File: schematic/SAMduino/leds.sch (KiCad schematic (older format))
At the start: 22 parts, among them SW1 SW_SPST, SW2 MCLR, SW3 SW_SPST, SW4 ERASE

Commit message: Specialty pins wired
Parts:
- removed J?: Conn_02x03_Odd_Even, symbol Connector_Generic:Conn_02x03_Odd_Even
- removed J?: Conn_02x02_Odd_Even, symbol Connector_Generic:Conn_02x02_Odd_Even
- removed J?: Conn_01x03, symbol Connector_Generic:Conn_01x03
- removed J?: Conn_02x04_Odd_Even, symbol Connector_Generic:Conn_02x04_Odd_Even
- removed J?: Conn_01x04, symbol Connector_Generic:Conn_01x04
- removed J?: Conn_02x10_Top_Bottom, symbol Connector_Generic:Conn_02x10_Top_Bottom
- added J? (x3): Conn_02x03_Odd_Even, symbol Connector_Generic:Conn_02x03_Odd_Even
- added J?: Conn_01x02, symbol Connector_Generic:Conn_01x02
- added J? (x2): Conn_02x02_Odd_Even, symbol Connector_Generic:Conn_02x02_Odd_Even
- added R? (x2): 100k, symbol Device:R
- added R? (x2): 4k7, symbol Device:R
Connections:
- net labels added: AN0, AN1, AN2, DAC0, NRST, PB5, RXD0, SPI0_MISO, SPI0_MOSI, SPI0_NPCS0, SPI0_SPCK, SWCLK, SWDIO, TWCK0, TWD0, TXD0, VDD5V, VIN
- net labels removed: MCLR
- wire segments 34 -> 89
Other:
- note added: "ADC and DAC"
- note added: "Power"
- note added: "Pullup Enable"
- note added: "TWI0"
- note added: "USART0"
- note removed: "ADC, DAC, Comparator?"
- note removed: "GPIO"
- note removed: "PWM"
- note removed: "TWI0 and TWI1\n(need pullups)"
- note removed: "USART0 and UART?"
- moved on the sheet: J?, R12, SW4

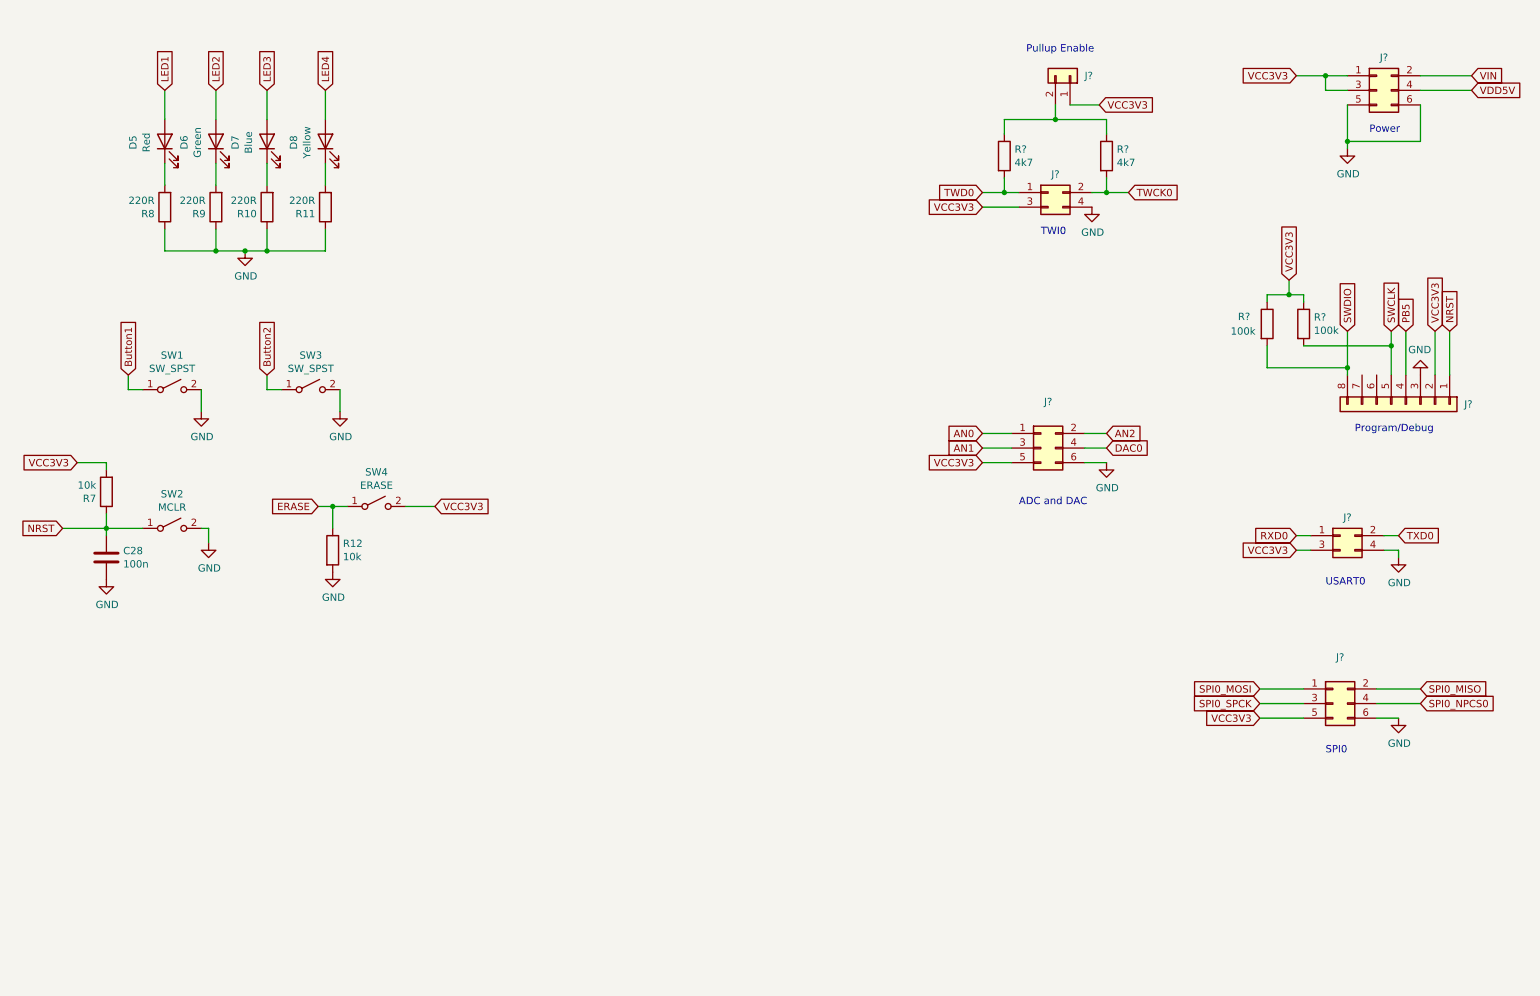
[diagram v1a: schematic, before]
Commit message: All pins connected
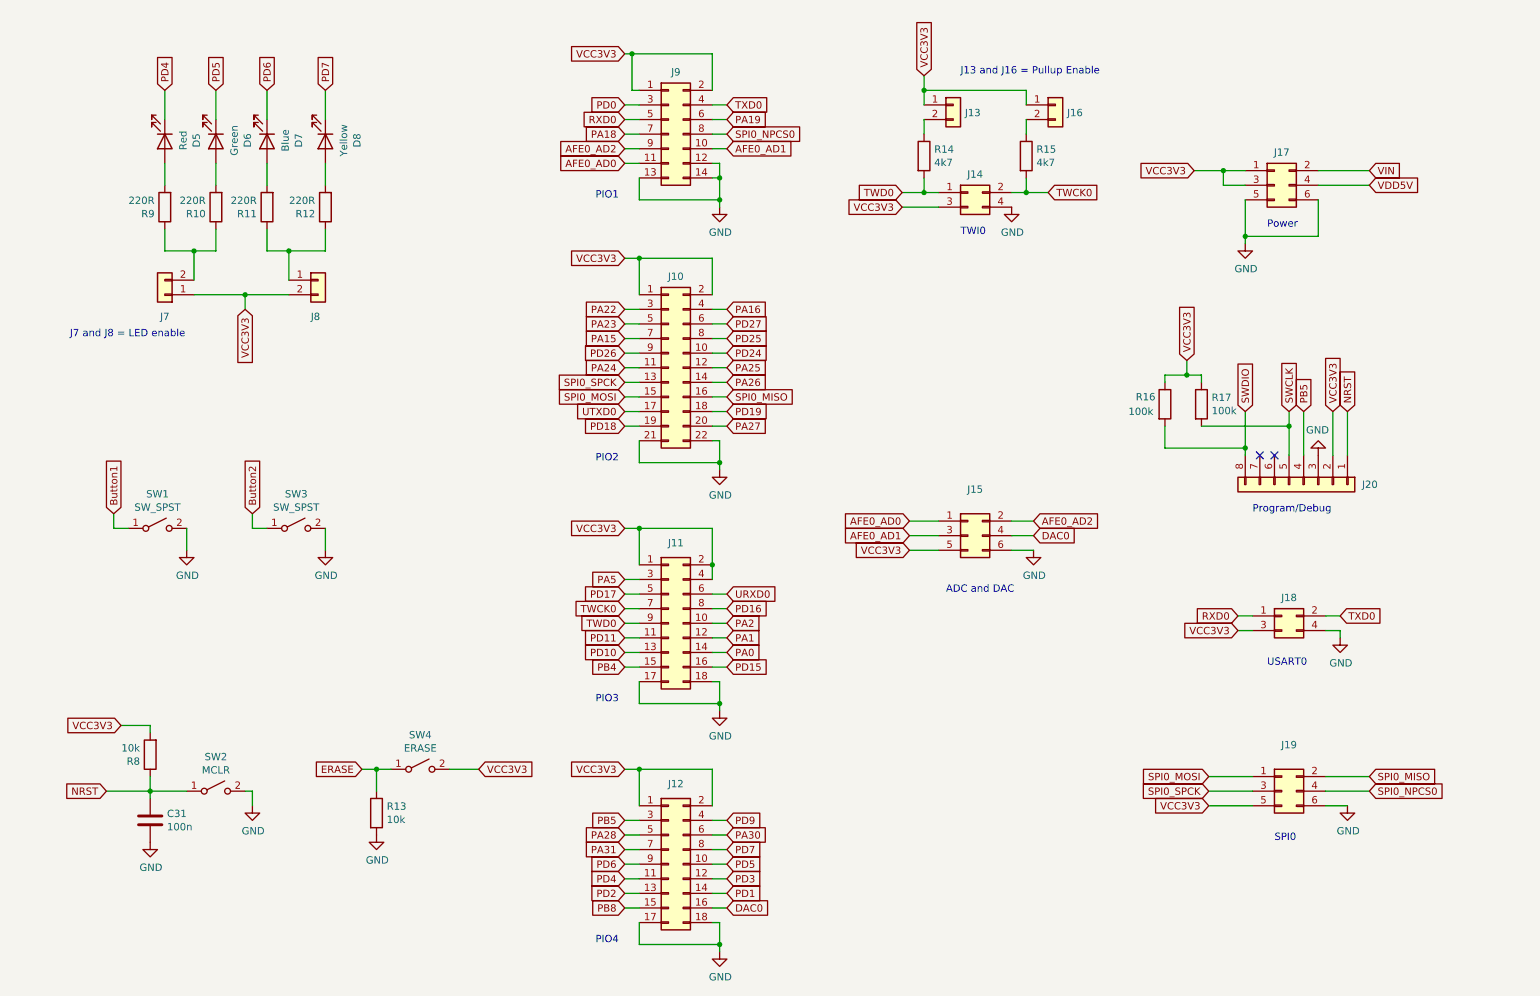
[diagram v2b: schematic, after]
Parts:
- removed J?: Conn_01x02, symbol Connector_Generic:Conn_01x02
- added J10: Conn_02x11_Odd_Even, symbol Connector_Generic:Conn_02x11_Odd_Even
- added J11, J12: Conn_02x09_Odd_Even, symbol Connector_Generic:Conn_02x09_Odd_Even
- added J13, J16, J7, J8: Conn_01x02, symbol Connector_Generic:Conn_01x02
- added J9: Conn_02x07_Odd_Even, symbol Connector_Generic:Conn_02x07_Odd_Even
- gave numbers to parts that had none: 10
- renumbered C28 to C31, R9 to R10, R10 to R11, R11 to R12, R12 to R13, R7 to R8, R8 to R9
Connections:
- net LED1 is gone; now on an unnamed net: D5.2 (A)
- net LED2 is gone; now on an unnamed net: D6.2 (A)
- net LED3 is gone; now on an unnamed net: D7.2 (A)
- net LED4 is gone; now on an unnamed net: D8.2 (A)
- net DAC0: now also J12.16 (Pin_16)
- net GND: now also J10.21 (Pin_21), J10.22 (Pin_22), J11.17 (Pin_17), J11.18 (Pin_18), J12.17 (Pin_17), J12.18 (Pin_18), J9.12 (Pin_12), J9.13 (Pin_13), J9.14 (Pin_14); no longer R10.1, R11.1, R12.1, R9.1
- net PB5: now also J12.3 (Pin_3)
- net RXD0: now also J9.5 (Pin_5)
- net SPI0_MISO: now also J10.16 (Pin_16)
- net SPI0_MOSI: now also J10.15 (Pin_15)
- net SPI0_NPCS0: now also J9.8 (Pin_8)
- net SPI0_SPCK: now also J10.13 (Pin_13)
- net TWCK0: now also J11.7 (Pin_7)
- net TWD0: now also J11.9 (Pin_9)
- net TXD0: now also J9.4 (Pin_4)
- net VCC3V3: now also J10.1 (Pin_1), J10.2 (Pin_2), J11.1 (Pin_1), J11.2 (Pin_2), J11.4 (Pin_4), J12.1 (Pin_1), J12.2 (Pin_2), J13.1 (Pin_1), J16.1 (Pin_1), J7.1 (Pin_1), J8.2 (Pin_2), J9.1 (Pin_1), J9.2 (Pin_2)
- net at R14.1: now also J13.2 (Pin_2); no longer R15.1
- net at R12.2: no longer D8.1 (K)
- net at R11.2: no longer D7.1 (K)
- net at R10.2: no longer D6.1 (K)
- net at R9.2: no longer D5.1 (K)
- net AN0 renamed AFE0_AD0
- net AFE0_AD0: now also J9.11 (Pin_11)
- net AN1 renamed AFE0_AD1
- net AFE0_AD1: now also J9.10 (Pin_10)
- net AN2 renamed AFE0_AD2
- net AFE0_AD2: now also J9.9 (Pin_9)
- new net: J16.2 (Pin_2), R15.1
- new net: J8.1 (Pin_1), R11.1, R12.1
- new net: J7.2 (Pin_2), R10.1, R9.1
- new net PA0: J11.14 (Pin_14)
- new net PA1: J11.12 (Pin_12)
- new net PA15: J10.7 (Pin_7)
- new net PA16: J10.4 (Pin_4)
- new net PA18: J9.7 (Pin_7)
- new net PA19: J9.6 (Pin_6)
- new net PA2: J11.10 (Pin_10)
- new net PA22: J10.3 (Pin_3)
- new net PA23: J10.5 (Pin_5)
- new net PA24: J10.11 (Pin_11)
- new net PA25: J10.12 (Pin_12)
- new net PA26: J10.14 (Pin_14)
- new net PA27: J10.20 (Pin_20)
- new net PA28: J12.5 (Pin_5)
- new net PA30: J12.6 (Pin_6)
- new net PA31: J12.7 (Pin_7)
- new net PA5: J11.3 (Pin_3)
- new net PB4: J11.15 (Pin_15)
- new net PB8: J12.15 (Pin_15)
- new net PD0: J9.3 (Pin_3)
- new net PD1: J12.14 (Pin_14)
- new net PD10: J11.13 (Pin_13)
- new net PD11: J11.11 (Pin_11)
- new net PD15: J11.16 (Pin_16)
- new net PD16: J11.8 (Pin_8)
- new net PD17: J11.5 (Pin_5)
- new net PD18: J10.19 (Pin_19)
- new net PD19: J10.18 (Pin_18)
- new net PD2: J12.13 (Pin_13)
- new net PD24: J10.10 (Pin_10)
- new net PD25: J10.8 (Pin_8)
- new net PD26: J10.9 (Pin_9)
- new net PD27: J10.6 (Pin_6)
- new net PD3: J12.12 (Pin_12)
- new net PD4: D5.1 (K), J12.11 (Pin_11)
- new net PD5: D6.1 (K), J12.10 (Pin_10)
- new net PD6: D7.1 (K), J12.9 (Pin_9)
- new net PD7: D8.1 (K), J12.8 (Pin_8)
- new net PD9: J12.4 (Pin_4)
- new net URXD0: J11.6 (Pin_6)
- new net UTXD0: J10.17 (Pin_17)
- no-connect marks 0 -> 2
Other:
- note added: "J13 and J16 = Pullup Enable"
- note added: "J7 and J8 = LED enable"
- note added: "PIO1"
- note added: "PIO2"
- note added: "PIO3"
- note added: "PIO4"
- note removed: "Pullup Enable"
- moved on the sheet: C31, D5, D6, D7, D8, J14, J15, J17, J18, J19, J20, R13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

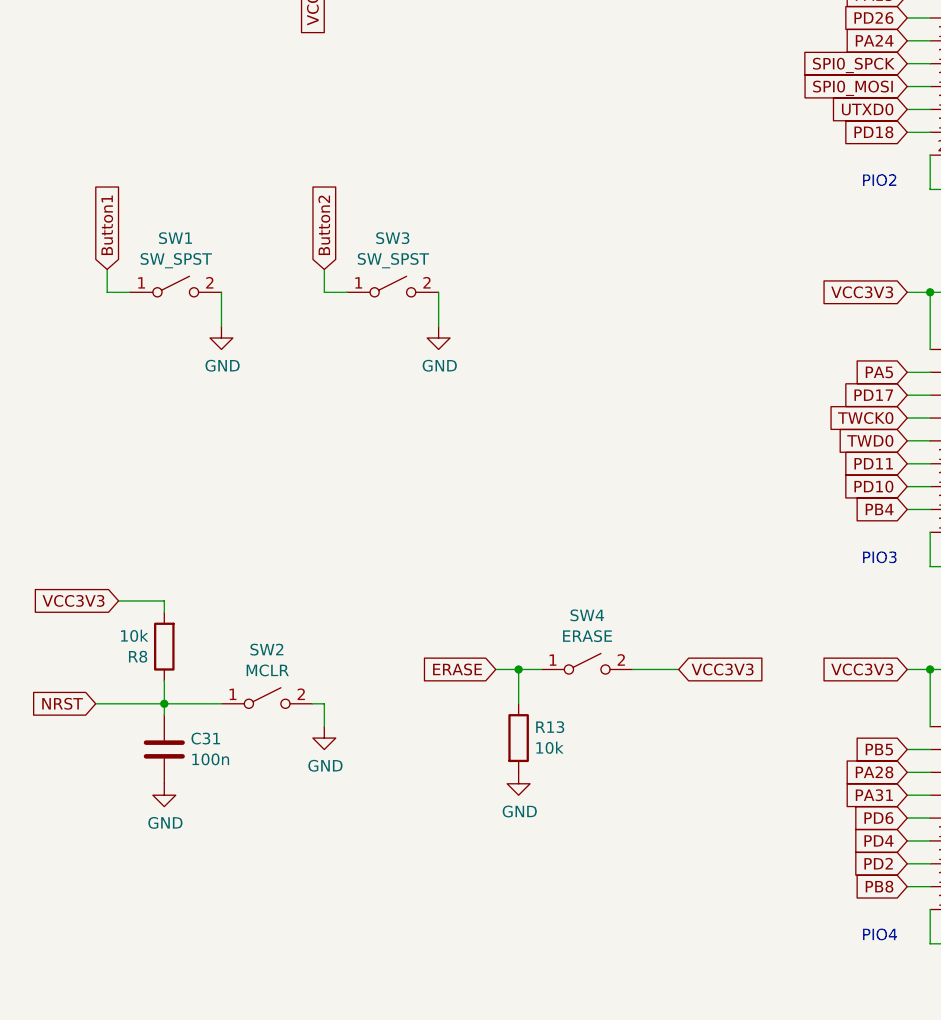
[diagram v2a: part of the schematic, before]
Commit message: Schematic with footprints
Some footprints need to be verified with actual components
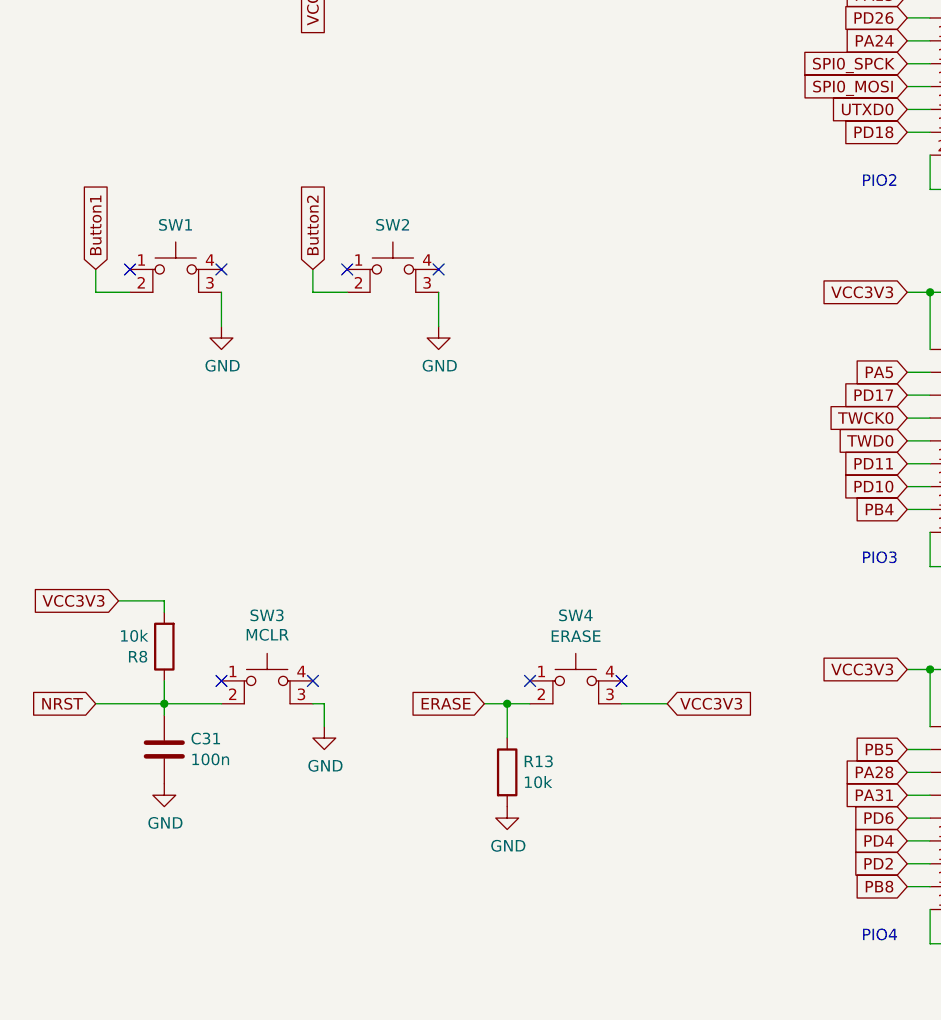
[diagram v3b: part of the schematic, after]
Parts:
- removed SW1, SW3: SW_SPST, symbol Switch:SW_SPST
- removed SW2: MCLR, symbol Switch:SW_SPST
- removed SW4: ERASE, symbol Switch:SW_SPST
- added SW1, SW2: SW_MEC_5E, SamacSys_Parts:FSM16JH, symbol Switch:SW_MEC_5E
- added SW3: MCLR, SamacSys_Parts:PTS647SK38SMTR2LFS, symbol Switch:SW_MEC_5E
- added SW4: ERASE, SamacSys_Parts:PTS647SK38SMTR2LFS, symbol Switch:SW_MEC_5E
- C31: footprint (none) -> Capacitor_SMD:C_0603_1608Metric
- D5, D6, D7, D8: footprint (none) -> LED_SMD:LED_0805_2012Metric
- J10: footprint (none) -> Connector_PinHeader_2.54mm:PinHeader_2x11_P2.54mm_Vertical
- J11, J12: footprint (none) -> Connector_PinHeader_2.54mm:PinHeader_2x09_P2.54mm_Vertical
- J13, J16, J7, J8: footprint (none) -> Connector_PinHeader_2.54mm:PinHeader_1x02_P2.54mm_Vertical
- J14, J18: footprint (none) -> Connector_PinHeader_2.54mm:PinHeader_2x02_P2.54mm_Vertical
- J15, J17, J19: footprint (none) -> Connector_PinHeader_2.54mm:PinHeader_2x03_P2.54mm_Vertical
- J20: footprint (none) -> Connector_PinHeader_2.54mm:PinHeader_1x08_P2.54mm_Horizontal
- J9: footprint (none) -> Connector_PinHeader_2.54mm:PinHeader_2x07_P2.54mm_Vertical
- R10, R11, R12, R13, R14, R15, R16, R17, R8, R9: footprint (none) -> Resistor_SMD:R_0603_1608Metric
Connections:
- net Button1: now also SW1.2
- net Button2: now also SW2.2
- net ERASE: now also SW4.2
- net GND: now also SW1.3 (K), SW2.3 (K), SW3.3 (K)
- net NRST: now also SW3.2
- net VCC3V3: now also SW4.3 (K)
- no-connect marks 2 -> 10
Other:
- moved on the sheet: R13

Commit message: Ready for PCB
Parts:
- removed C31: 100n, Capacitor_SMD:C_0603_1608Metric, symbol Device:C
- R8: value 10k -> 100k
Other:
- note added: "Do the buttons need a series current limiting resistor"
- moved on the sheet: R8, SW3
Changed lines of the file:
@@
 L Device:R R8
 U 1 1 61656110
-P 1450 5600
-F 0 "R8" H 1520 5646 50  0000 L CNN
-F 1 "10k" H 1520 5555 50  0000 L CNN
-F 2 "Resistor_SMD:R_0603_1608Metric" V 1380 5600 50  0001 C CNN
-F 3 "~" H 1450 5600 50  0001 C CNN
-	1    1450 5600
+P 1450 5800
+F 0 "R8" H 1520 5846 50  0000 L CNN
+F 1 "100k" H 1520 5755 50  0000 L CNN
+F 2 "Resistor_SMD:R_0603_1608Metric" V 1380 5800 50  0001 C CNN
+F 3 "~" H 1450 5800 50  0001 C CNN
+	1    1450 5800
 	-1   0    0    1
 $EndComp
@@
 F 3 "~" H 2950 6150 50  0001 C CNN
 	1    2950 6150
-	1    0    0    -1
-$EndComp
-$Comp
-L Device:C C31
-U 1 1 61610082
-P 1450 6050
-F 0 "C31" H 1565 6096 50  0000 L CNN
-F 1 "100n" H 1565 6005 50  0000 L CNN
-F 2 "Capacitor_SMD:C_0603_1608Metric" H 1488 5900 50  0001 C CNN
-F 3 "~" H 1450 6050 50  0001 C CNN
-	1    1450 6050
 	1    0    0    -1
 $EndComp
@@
 L power:GND #PWR040
 U 1 1 6163E102
-P 2150 5950
-F 0 "#PWR040" H 2150 5700 50  0001 C CNN
-F 1 "GND" H 2155 5777 50  0000 C CNN
-F 2 "" H 2150 5950 50  0001 C CNN
-F 3 "" H 2150 5950 50  0001 C CNN
-	1    2150 5950
-	1    0    0    -1
-$EndComp
-$Comp
-L power:GND #PWR038
-U 1 1 6163E713
-P 1450 6200
-F 0 "#PWR038" H 1450 5950 50  0001 C CNN
-F 1 "GND" H 1455 6027 50  0000 C CNN
-F 2 "" H 1450 6200 50  0001 C CNN
-F 3 "" H 1450 6200 50  0001 C CNN
-	1    1450 6200
-	1    0    0    -1
-$EndComp
-Text GLabel 1250 5400 0    50   Input ~ 0
-VCC3V3
-Text GLabel 1150 5850 0    50   Input ~ 0
+P 2150 6150
+F 0 "#PWR040" H 2150 5900 50  0001 C CNN
+F 1 "GND" H 2155 5977 50  0000 C CNN
+F 2 "" H 2150 6150 50  0001 C CNN
+F 3 "" H 2150 6150 50  0001 C CNN
+	1    2150 6150
+	1    0    0    -1
+$EndComp
+Text GLabel 1250 5600 0    50   Input ~ 0
+VCC3V3
+Text GLabel 1150 6050 0    50   Input ~ 0
 NRST
 Wire Wire Line
-	2100 5850 2150 5850
-Wire Wire Line
-	2150 5850 2150 5950
-Wire Wire Line
-	1150 5850 1450 5850
-Wire Wire Line
-	1450 5900 1450 5850
-Connection ~ 1450 5850
-Wire Wire Line
-	1450 5850 1700 5850
-Wire Wire Line
-	1450 5750 1450 5850
-Wire Wire Line
-	1250 5400 1450 5400
-Wire Wire Line
-	1450 5400 1450 5450
+	2100 6050 2150 6050
+Wire Wire Line
+	2150 6050 2150 6150
+Wire Wire Line
+	1150 6050 1450 6050
+Wire Wire Line
+	1450 5950 1450 6050
+Wire Wire Line
+	1250 5600 1450 5600
+Wire Wire Line
+	1450 5600 1450 5650
 Text GLabel 3650 5850 2    50   Input ~ 0
 VCC3V3
@@
 L Switch:SW_MEC_5E SW3
 U 1 1 616B6278
-P 1900 5850
-F 0 "SW3" H 1900 6235 50  0000 C CNN
-F 1 "MCLR" H 1900 6150 50  0000 C CNN
-F 2 "SamacSys_Parts:PTS647SK38SMTR2LFS" H 1900 6150 50  0001 C CNN
-F 3 "http://www.apem.com/int/index.php?controller=attachment&id_attachment=1371" H 1900 6150 50  0001 C CNN
-	1    1900 5850
+P 1900 6050
+F 0 "SW3" H 1900 6435 50  0000 C CNN
+F 1 "MCLR" H 1900 6350 50  0000 C CNN
+F 2 "SamacSys_Parts:PTS647SK38SMTR2LFS" H 1900 6350 50  0001 C CNN
+F 3 "http://www.apem.com/int/index.php?controller=attachment&id_attachment=1371" H 1900 6350 50  0001 C CNN
+	1    1900 6050
 	1    0    0    -1
 $EndComp
@@
 Wire Wire Line
 	2100 4050 2100 3950
-NoConn ~ 1700 5750
-NoConn ~ 2100 5750
+NoConn ~ 1700 5950
+NoConn ~ 2100 5950
 NoConn ~ 3050 5750
 NoConn ~ 3450 5750
@@
 NoConn ~ 2250 3950
 NoConn ~ 2650 3950
+Connection ~ 1450 6050
+Wire Wire Line
+	1450 6050 1700 6050
+Text Notes 950  4800 0    50   ~ 0
+Do the buttons need a series current limiting resistor
 $EndSCHEMATC

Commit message: Changed MCP2221 RST connection
Removed some comments
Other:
- note removed: "Do the buttons need a series current limiting resistor"
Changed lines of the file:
@@
 Wire Wire Line
 	1450 6050 1700 6050
-Text Notes 950  4800 0    50   ~ 0
-Do the buttons need a series current limiting resistor
 $EndSCHEMATC
